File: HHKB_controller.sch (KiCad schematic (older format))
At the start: 62 parts, among them CN1 CONN_15, CN2 CONN_13, J1 USB_B, P1 CONN_1, P10 CONN_1, P100 CONN_3X2, P11 CONN_1, P12 CONN_1, P13 CONN_1, P14 CONN_1, P15 CONN_1, P16 CONN_1, P17 CONN_1, P18 CONN_1, P19 CONN_1, P2 CONN_1, P20 CONN_1, P21 CONN_1, P22 CONN_1, P23 CONN_1, P24 CONN_1, P25 CONN_1, P26 CONN_1, P27 CONN_1, P28 CONN_1, P29 CONN_1, P3 CONN_1, P30 CONN_1, P31 CONN_1, P32 CONN_1, P33 CONN_1, P34 CONN_1, P35 CONN_1, P36 CONN_1, P37 CONN_1, P38 CONN_1, P39 CONN_1, P4 CONN_1, P5 CONN_1, P6 CONN_1, P7 CONN_1, P8 CONN_1, P9 CONN_1, SW1 SW_PUSH, U1 ATMEGA32U4, X1 16MHz

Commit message: Add Bluetooth module part
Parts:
- removed J1: USB_B, symbol USB_MINIB
- removed P10, P11, P12, P13, P15, P16, P17, P20, P21, P22, P23, P24, P25, P28, P29, P31, P34, P35, P36, P37, P38, P39: CONN_1, symbol CONN_1
- added C10: 0.1u, symbol C
- added J1: USB_MINI_MICRO_B, symbol USB_MINI_MICRO_B
- added JP2, JP4: JUMPER, symbol JUMPER
- added Q2: MOSFET_N, symbol MOSFET_N
- added R15: 10K, symbol R
- renumbered C9 to C2, C2 to C3, C3 to C4, C4 to C5, C5 to C6, C6 to C7, C7 to C8, C8 to C9, P33 to P10, P32 to P11, P19 to P12, P18 to P13, P100 to P15, R3 to R1, R1 to R2, R2 to R3
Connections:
- net labels added: BT_DTR, BT_INDICATOR, BT_RX, BT_TX, HHKB_GND
- wire segments 162 -> 161
- no-connect marks 0 -> 8
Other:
- note added: "AMP MEASURE POINT"
- note added: "For Bluetooth via UART"
- note added: "For Debug"
- note added: "For Power Control"
- note added: "HHKB Matrix Power Control"
- note added: "Normally On\nLow = Off"
- note added: "Optional Pullup Resistors"
- note added: "UART connection of Bluetooth Module"
- note removed: "Controller I/O Pins"
- note removed: "Pullup Resistors"
- moved on the sheet: C2, CN1, CN2, P1, P10, P11, P12, P13, P2, P3, P4, P5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

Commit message: Finish Rev. A
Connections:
- net labels added: BT_LIPO
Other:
- moved on the sheet: JP1, P30

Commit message: Fix USB controller part
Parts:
- removed P30, P5: CONN_1, symbol CONN_1
- removed R1: 1K, symbol R
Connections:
- wire segments 161 -> 156
- no-connect marks 8 -> 6
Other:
- note added: "Hirose DF14A for JP"
- note added: "ICSP"
- note added: "JST ZH for Pro2"
- note removed: "Hirose PH for Pro"
- note removed: "Hirose ZH for Pro2"
- note removed: "ISP pins"
- note removed: "Optional Pullup Resistors"
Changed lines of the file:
@@
 	-1   0    0    1
 $EndComp
-$Comp
-L R R1
-U 1 1 517F6E00
-P 3550 6250
-F 0 "R1" V 3630 6250 50  0000 C CNN
-F 1 "1K" V 3550 6250 50  0000 C CNN
-F 2 "" H 3550 6250 60  0000 C CNN
-F 3 "" H 3550 6250 60  0000 C CNN
-	1    3550 6250
-	0    -1   -1   0
-$EndComp
-$Comp
-L +5V #PWR018
-U 1 1 517F6E08
-P 3000 6100
-F 0 "#PWR018" H 3000 6190 20  0001 C CNN
-F 1 "+5V" H 3000 6190 30  0000 C CNN
-F 2 "" H 3000 6100 60  0000 C CNN
-F 3 "" H 3000 6100 60  0000 C CNN
-	1    3000 6100
-	1    0    0    -1
-$EndComp
-Text Label 3900 6250 0    60   ~ 0
-PD7
-Text Notes 2950 6600 0    60   Italic 0
-Optional Pullup Resistors
 Text Notes 900  3000 0    60   Italic 0
 USB pins for external connector
@@
 $EndComp
 Text Notes 1800 5900 0    60   Italic 0
-Hirose ZH for Pro2
+JST ZH for Pro2
 Text Label 2550 4600 0    60   Italic 0
 PB0
@@
 	-1   0    0    -1
 $EndComp
+Text Label 1500 4500 0    60   Italic 0
+PB0
 Text Label 1500 4600 0    60   Italic 0
-PB0
+PB1
 Text Label 1500 4700 0    60   Italic 0
-PB1
+PB2
 Text Label 1500 4800 0    60   Italic 0
-PB2
+PB3
 Text Label 1500 4900 0    60   Italic 0
-PB3
+PB4
 Text Label 1500 5000 0    60   Italic 0
-PB4
+PB5
 Text Label 1500 5100 0    60   Italic 0
-PB5
-Text Label 1500 5200 0    60   Italic 0
 PB6
-Text Label 1500 4500 0    60   Italic 0
+Text Label 1500 4400 0    60   Italic 0
 PB7
-Text Label 1500 4400 0    60   Italic 0
+Text Label 1500 4300 0    60   Italic 0
 PD7
 $Comp
@@
 	1    0    0    -1
 $EndComp
-Text Notes 750  5900 0    60   Italic 0
-Hirose PH for Pro
+Text Notes 650  5900 0    60   Italic 0
+Hirose DF14A for JP
 $Comp
 L +5V #PWR021
@@
 $EndComp
 $Comp
-L CONN_1 P5
-U 1 1 519EBF68
-P 7100 5000
-F 0 "P5" H 7180 5000 40  0000 L CNN
-F 1 "CONN_1" H 7100 5055 30  0001 C CNN
-F 2 "" H 7100 5000 60  0000 C CNN
-F 3 "" H 7100 5000 60  0000 C CNN
-	1    7100 5000
-	-1   0    0    1
-$EndComp
-$Comp
 L CONN_1 P7
 U 1 1 519EBF83
@@
 	-1   0    0    1
 $EndComp
-Text Label 7300 5000 0    60   ~ 0
-VBUS
 Text Label 7300 5200 0    60   ~ 0
 PD2
@@
 	1    0    0    -1
 $EndComp
-Text Notes 9850 7050 0    60   Italic 0
-ISP pins
+Text Notes 9950 6850 0    60   Italic 0
+ICSP
 $Comp
 L CONN_3X2 P15
@@
 For Bluetooth via UART
 NoConn ~ 5650 3500
-NoConn ~ 7800 2700
-NoConn ~ 7800 2600
 NoConn ~ 7800 2200
 NoConn ~ 7800 2100
@@
 AMP MEASURE POINT
 $Comp
-L CONN_1 P30
-U 1 1 51BB5FB5
-P 1150 3250
-F 0 "P30" H 1230 3250 40  0000 L CNN
-F 1 "CONN_1" H 1150 3305 30  0001 C CNN
-F 2 "" H 1150 3250 60  0000 C CNN
-F 3 "" H 1150 3250 60  0000 C CNN
-	1    1150 3250
-	-1   0    0    1
-$EndComp
-Text Notes 900  3450 0    60   Italic 0
-AMP MEASURE POINT
-$Comp
 L JUMPER JP4
 U 1 1 51BC02F3
@@
 	1    2500 6900
 	0    -1   -1   0
-$EndComp
-$Comp
-L GND #PWR029
-U 1 1 51BC03C8
-P 2500 7250
-F 0 "#PWR029" H 2500 7250 30  0001 C CNN
-F 1 "GND" H 2500 7180 30  0001 C CNN
-F 2 "" H 2500 7250 60  0000 C CNN
-F 3 "" H 2500 7250 60  0000 C CNN
-	1    2500 7250
-	1    0    0    -1
 $EndComp
 Text GLabel 5600 5550 2    60   Input ~ 0
@@
 VBUS
 Wire Wire Line
-	3300 6250 3000 6250
-Wire Wire Line
 	1300 2825 1600 2825
 Wire Wire Line
@@
 	8700 5200 9000 5200
 Wire Wire Line
-	3800 6250 4100 6250
-Wire Wire Line
 	9850 3300 9850 3200
 Wire Wire Line
@@
 	9800 5300 10100 5300
 Wire Wire Line
+	1250 4300 1700 4300
+Wire Wire Line
 	1250 4400 1700 4400
 Wire Wire Line
@@
 Wire Wire Line
 	1250 5100 1700 5100
-Wire Wire Line
-	1250 5200 1700 5200
-Wire Wire Line
-	1450 3950 1450 4300
 Wire Wire Line
 	1250 4100 1450 4100
@@
 Wire Wire Line
 	1250 4200 1450 4200
-Connection ~ 1450 4200
-Wire Wire Line
-	1450 4300 1250 4300
-Wire Wire Line
-	1450 5300 1450 5650
+Wire Wire Line
+	1450 5200 1450 5650
 Wire Wire Line
 	1250 5300 1450 5300
 Wire Wire Line
-	1250 5400 1450 5400
-Connection ~ 1450 5400
-Wire Wire Line
-	1250 5500 1450 5500
-Connection ~ 1450 5500
-Wire Wire Line
 	5200 1000 5200 1500
 Wire Wire Line
@@
 Wire Wire Line
 	7250 5400 7550 5400
-Wire Wire Line
-	7250 5000 7550 5000
-Wire Wire Line
-	3000 6250 3000 6100
 Wire Wire Line
 	3400 6900 3400 6850
@@
 Connection ~ 2500 6550
 Wire Wire Line
+	5600 5550 5200 5550
+Wire Wire Line
+	1600 1500 3400 1500
+Wire Wire Line
+	5600 5350 5200 5350
+Wire Wire Line
+	5400 2000 5650 2000
+Wire Wire Line
+	2200 900  2450 900
+Wire Wire Line
+	1950 1050 1550 1050
+$Comp
+L GND #PWR030
+U 1 1 52AACE12
+P 2500 7250
+F 0 "#PWR030" H 2500 7250 30  0001 C CNN
+F 1 "GND" H 2500 7180 30  0001 C CNN
+F 2 "" H 2500 7250 60  0000 C CNN
+F 3 "" H 2500 7250 60  0000 C CNN
+	1    2500 7250
+	1    0    0    -1
+$EndComp
+Wire Wire Line
 	2500 7200 2500 7250
 Wire Wire Line
-	5600 5550 5200 5550
-Wire Wire Line
-	1600 1500 3400 1500
-Wire Wire Line
-	5600 5350 5200 5350
-Wire Wire Line
-	5400 2000 5650 2000
-Wire Wire Line
-	2200 900  2450 900
-$Comp
-L +5V #PWR030
-U 1 1 51BEA767
-P 1500 3250
-F 0 "#PWR030" H 1500 3340 20  0001 C CNN
-F 1 "+5V" H 1500 3340 30  0000 C CNN
-F 2 "" H 1500 3250 60  0000 C CNN
-F 3 "" H 1500 3250 60  0000 C CNN
-	1    1500 3250
-	0    1    1    0
-$EndComp
-Wire Wire Line
-	1500 3250 1300 3250
-Wire Wire Line
-	1950 1050 1550 1050
+	1450 4200 1450 3950
+Wire Wire Line
+	1250 5200 1450 5200
+Connection ~ 1450 5300
+Wire Wire Line
+	1250 5400 1700 5400
+Wire Wire Line
+	1250 5500 1700 5500
+Text Label 1500 5400 0    60   ~ 0
+PC6
+Text Label 1500 5500 0    60   ~ 0
+PC7
 $EndSCHEMATC

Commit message: Add Power Source Selector
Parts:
- removed JP1: JUMPER3, symbol JUMPER3
- removed P10, P11, P6, P7, P8, P9: CONN_1, symbol CONN_1
- added F1: PPTC, symbol PPTC
- added JP1, JP5: JUMPER, symbol JUMPER
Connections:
- net labels added: 5V_BOOST, BT_CTS, BT_RTS, LIPO_SENSE, VUSB
- net labels removed: BT_DTR, BT_LIPO, VBUS, VIN
- wire segments 156 -> 154
- no-connect marks 6 -> 5
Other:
- note added: "Amp Measure"
- note added: "Bluetooth Extension"
- note added: "HHKB Matrix Interface"
- note added: "No Boost"
- note added: "No PPTC"
- note added: "No Power Control"
- note added: "Optional"
- note added: "Optional\nTeensy compatible LED"
- note added: "Program and Debug"
- note added: "USB keyboard configurations:\n 1)Close "No Power Control" and\n 3)close "No Boost" jumper to use raw USB power.\n Optionally you can boost into 5V\n with making "No Boost" open and "No LIPO" closed."
- note added: "USB pinouts for external connector"
- note removed: "AMP MEASURE POINT"
- note removed: "Extension connector"
- note removed: "For Bluetooth via UART"
- note removed: "For Power Control"
- note removed: "Optional Teensy compatible LED"
- note removed: "Optional capacitor"
- note removed: "UART connection of Bluetooth Module"
- note removed: "USB pins for external connector"
- moved on the sheet: C10, C2, CN1, CN2, D1, JP2, JP4, P12, P13, P14, P15, P26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

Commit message: Design initial Rev.B PCB
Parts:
- added JP10: JUMPER, symbol JUMPER
- added P11, P12: CONN_1, symbol CONN_1
- renumbered JP2 to JP11, JP5 to JP2, JP4 to JP3, P27 to P10, P12 to P5, P13 to P6, P14 to P7, P15 to P8, P26 to P9, F1 to PPTC1
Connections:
- net labels added: 5V_SOURCE, VUSB_RAW
- wire segments 154 -> 161

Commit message: Fix missing symbol in schematic
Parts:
- removed J1: USB_MINI_MICRO_B, symbol USB_MINI_MICRO_B
- added J1: USB_mini_micro_B, symbol USB_mini_micro_B
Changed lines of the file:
@@
 Text Label 6450 6650 2    60   ~ 0
 PD5
-$Comp
-L USB_MINI_MICRO_B J1
-U 1 1 51B937B1
-P 1450 1650
-F 0 "J1" H 1050 1600 60  0000 C CNN
-F 1 "USB_MINI_MICRO_B" H 1300 1900 60  0001 C CNN
-F 2 "" H 1400 1650 60  0000 C CNN
-F 3 "" H 1400 1650 60  0000 C CNN
-	1    1450 1650
-	1    0    0    -1
-$EndComp
 NoConn ~ 1600 1800
 $Comp
@@
 	0    -1   -1   0
 $EndComp
+$Comp
+L USB_mini_micro_B J1
+U 1 1 53485EB0
+P 1450 1650
+F 0 "J1" H 1050 1600 60  0000 C CNN
+F 1 "USB_mini_micro_B" H 1300 1900 60  0001 C CNN
+F 2 "" H 1400 1650 60  0000 C CNN
+F 3 "" H 1400 1650 60  0000 C CNN
+	1    1450 1650
+	1    0    0    -1
+$EndComp
 $EndSCHEMATC

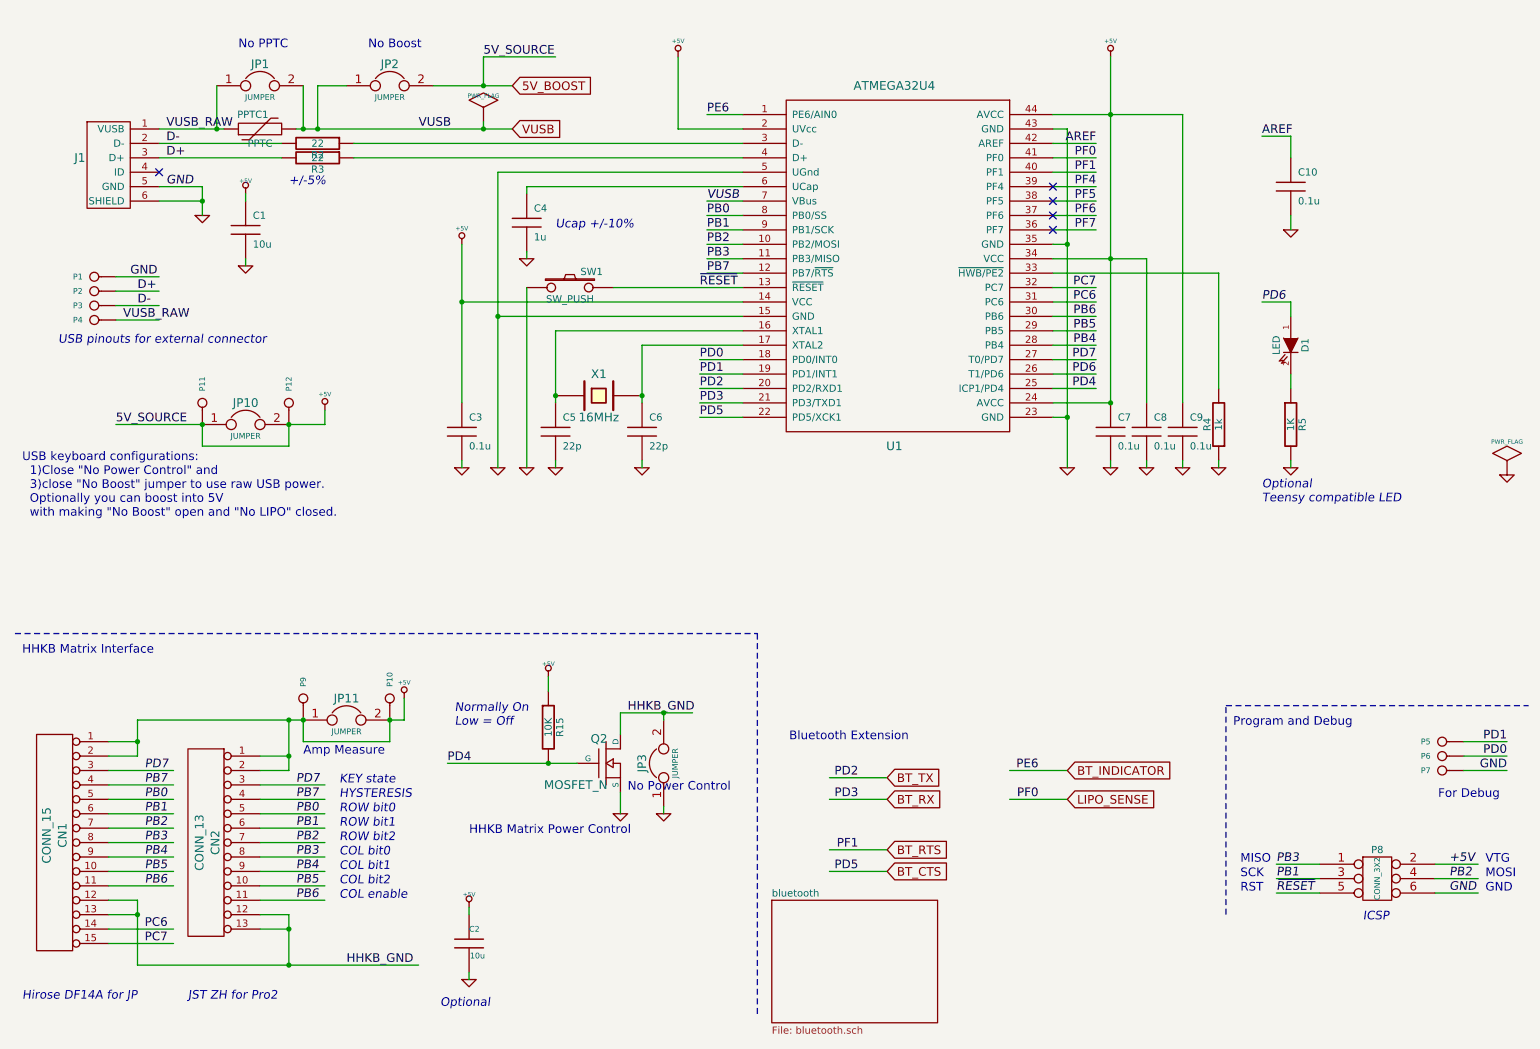
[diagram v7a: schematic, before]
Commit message: Fix many fixes of rev.B errata
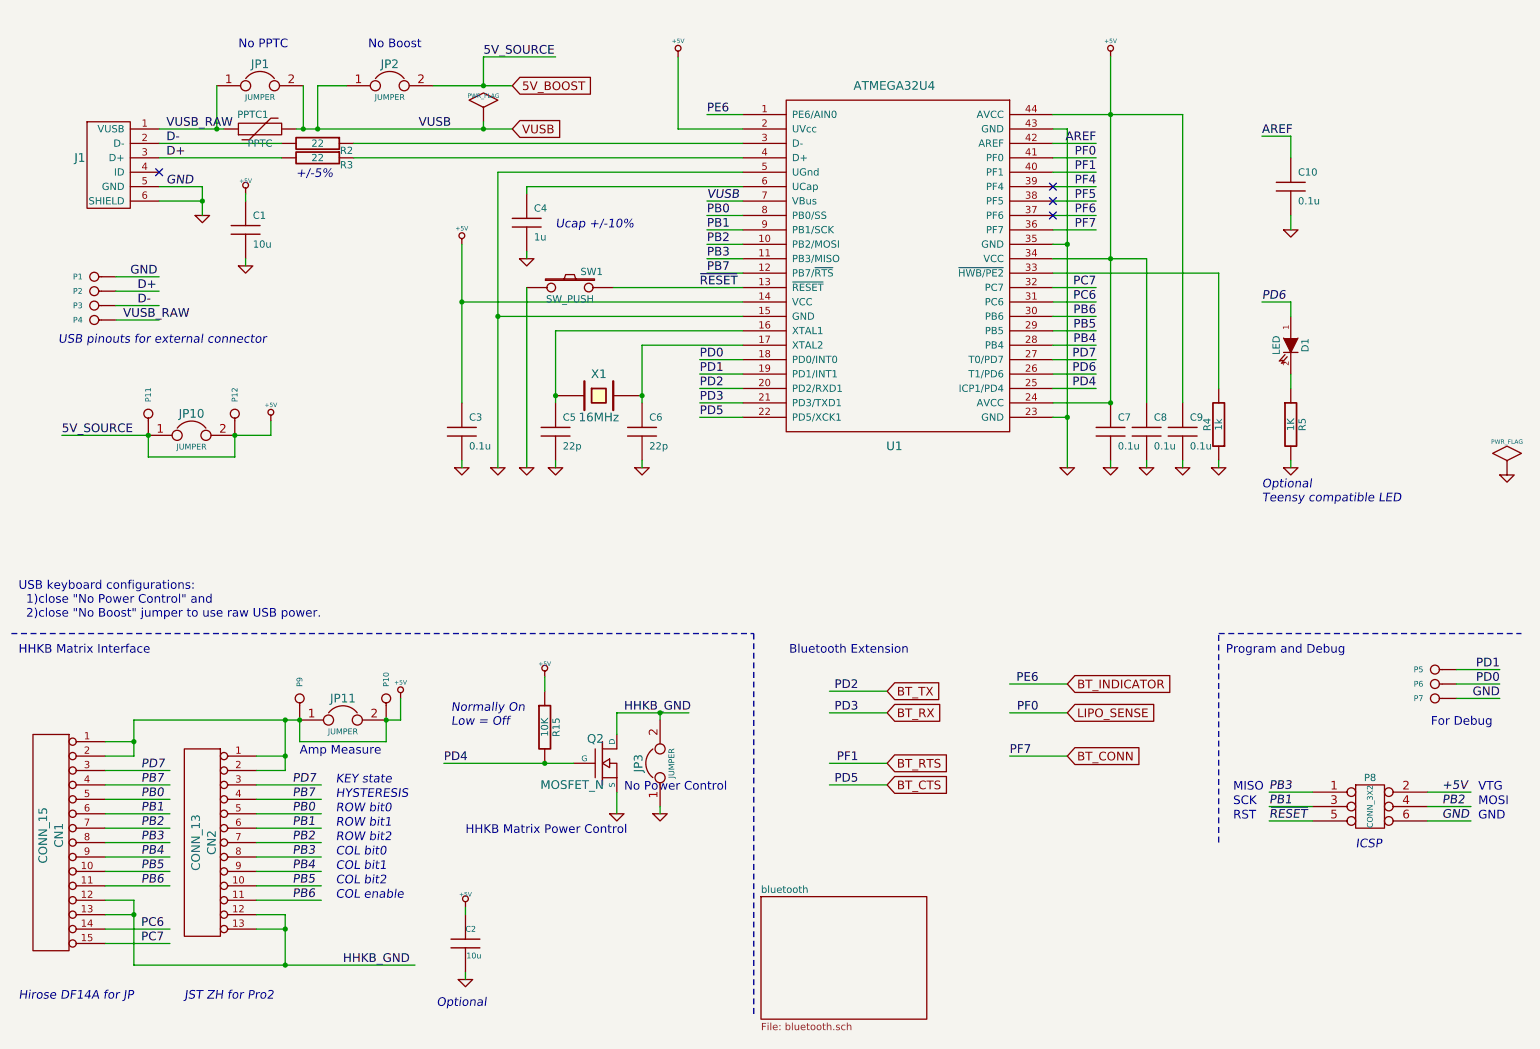
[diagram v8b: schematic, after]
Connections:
- net labels added: BT_CONN
- wire segments 161 -> 162
- no-connect marks 5 -> 4
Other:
- note added: "USB keyboard configurations:\n 1)close "No Power Control" and\n 2)close "No Boost" jumper to use raw USB power."
- note removed: "USB keyboard configurations:\n 1)Close "No Power Control" and\n 3)close "No Boost" jumper to use raw USB power.\n Optionally you can boost into 5V\n with making "No Boost" open and "No LIPO" closed."
- moved on the sheet: C2, CN1, CN2, JP10, JP11, JP3, P10, P11, P12, P5, P6, P7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
